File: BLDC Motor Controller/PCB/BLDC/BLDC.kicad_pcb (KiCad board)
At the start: 2 copper layers, 106.2 x 82.3 mm, 34 parts, among them J1 Screw_Terminal_01x03, J2 Screw_Terminal_01x02, J3 Conn_01x03_Socket, Q1 IRLZ44N, Q2 IRLZ44N, Q3 IRLZ44N, Q4 IRLZ44N, Q5 IRLZ44N, Q6 IRLZ44N, U1 IR2101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

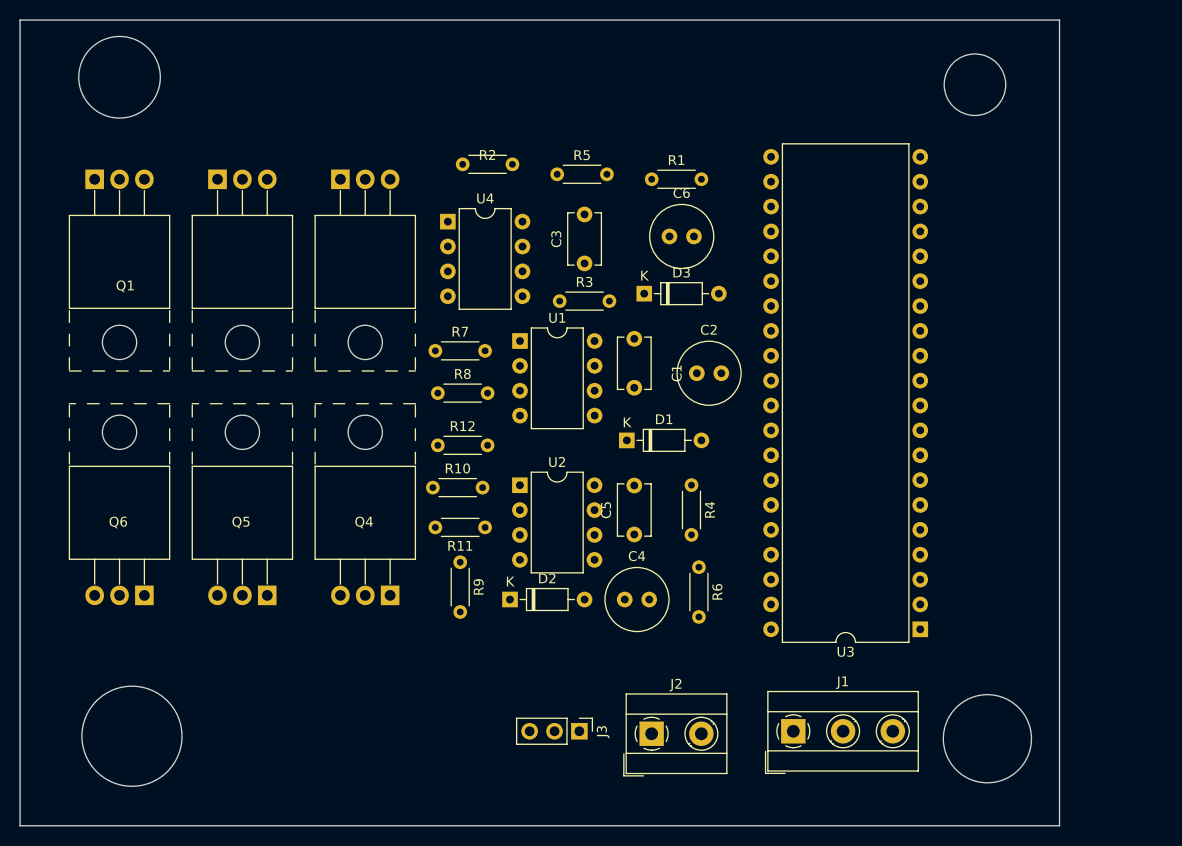
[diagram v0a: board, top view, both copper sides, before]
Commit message: Added Kalman Filter for MPU6050.
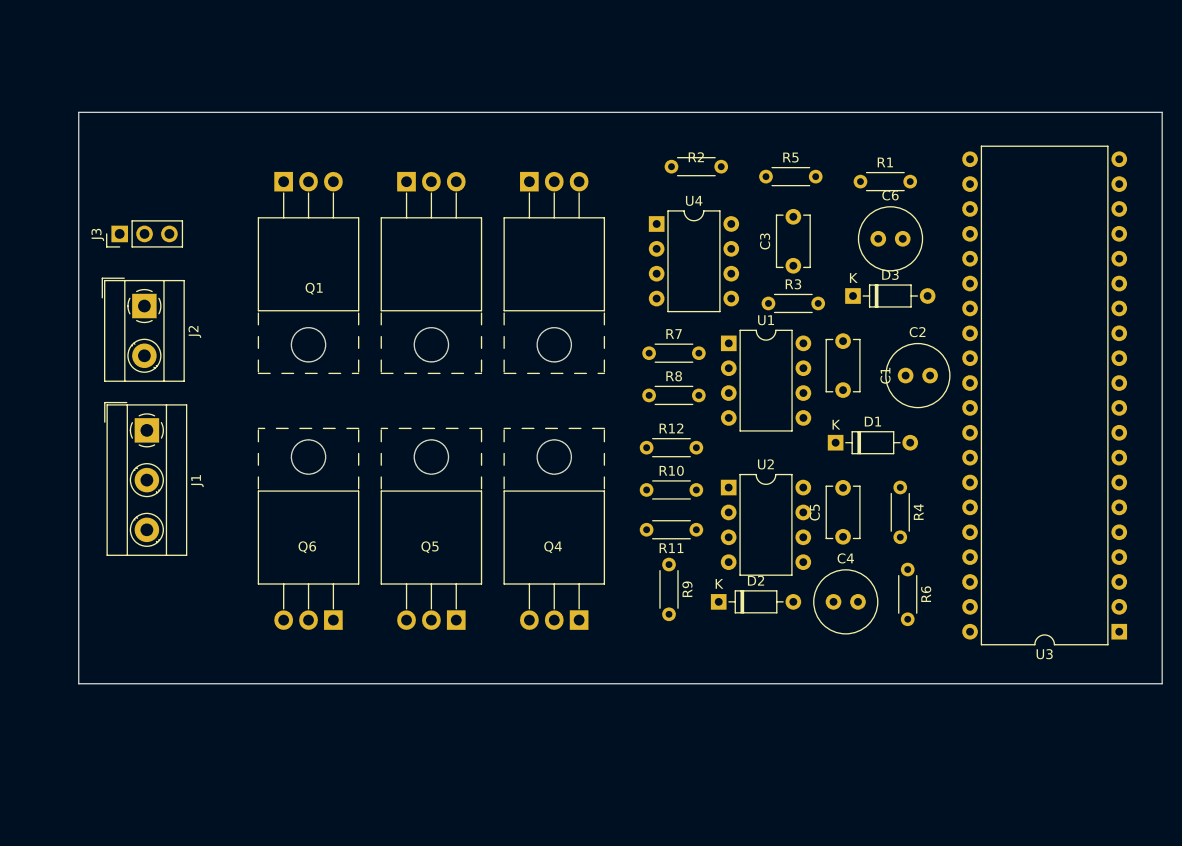
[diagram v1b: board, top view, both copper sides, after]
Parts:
- moved J1 72.8 mm to (54.4, 71.6), turned to -90 degrees
- moved J3 69.2 mm to (51.6, 51.6), turned to 90 degrees
- moved J2 67.8 mm to (54.1, 58.9), turned to -90 degrees
- moved R10 21.8 mm to (105.4, 77.7)
- moved R7 21.8 mm to (105.7, 63.7)
- moved R11 21.6 mm to (110.5, 81.8)
- moved R8 21.6 mm to (105.7, 68.1)
- moved C6 21.3 mm to (129.1, 52.1)
- moved D2 21.3 mm to (112.8, 89.1)
- moved R12 21.3 mm to (105.4, 73.4)
- moved R3 21.3 mm to (117.8, 58.7)
- moved R9 21.3 mm to (107.7, 85.3)
- moved U1 21.3 mm to (113.8, 62.7)
- moved U4 21.3 mm to (106.4, 50.5)
- moved C1 21.3 mm to (125.5, 62.5)
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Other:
- board size 106.2 x 82.3 mm -> 110.7 x 58.4 mm
